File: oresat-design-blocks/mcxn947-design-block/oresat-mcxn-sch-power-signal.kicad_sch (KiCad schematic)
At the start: 64 parts, among them J1 BKUP-BATT, J3 CAN, J4 TERM, J5 10pin ARM SWD, J6 FTDI-UART-6PIN, SW1 RESET, SW2 ISP(BOOT), U1 MCXN947VKLT, U2 TCAN330, U3 TPS62111RSA, Y1 24 MHz, Y2 32.768 KHz

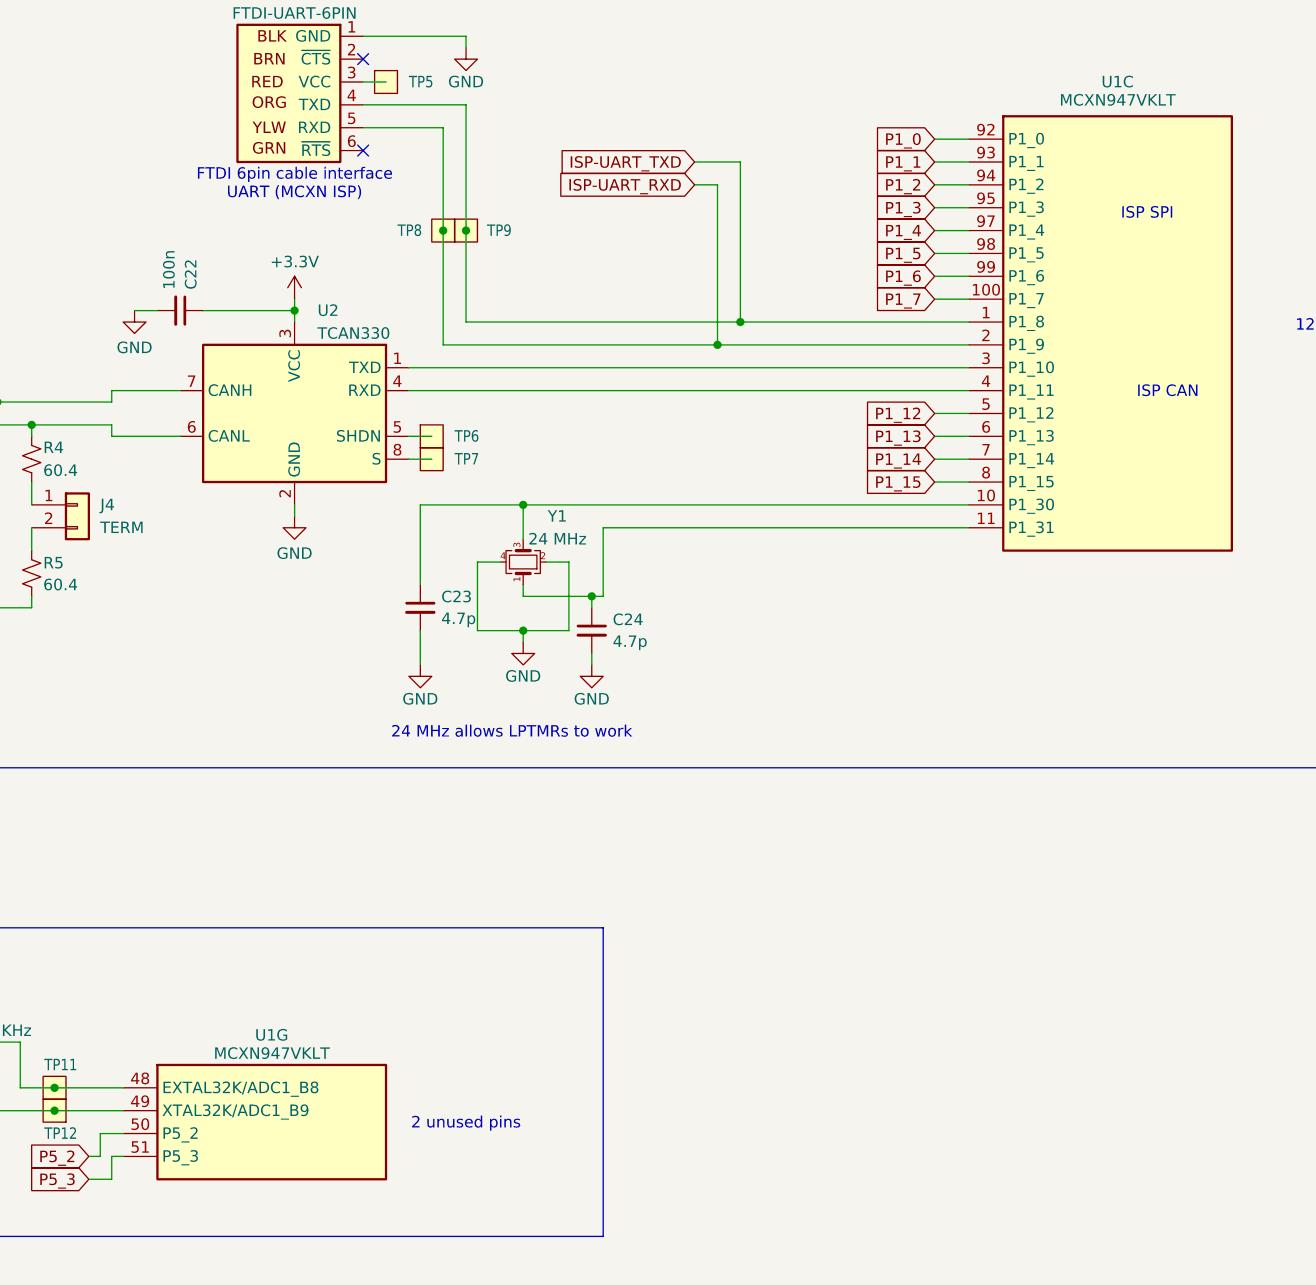
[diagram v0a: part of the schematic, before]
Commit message: updated MCXN board with new cap footprints, cleaned up routes
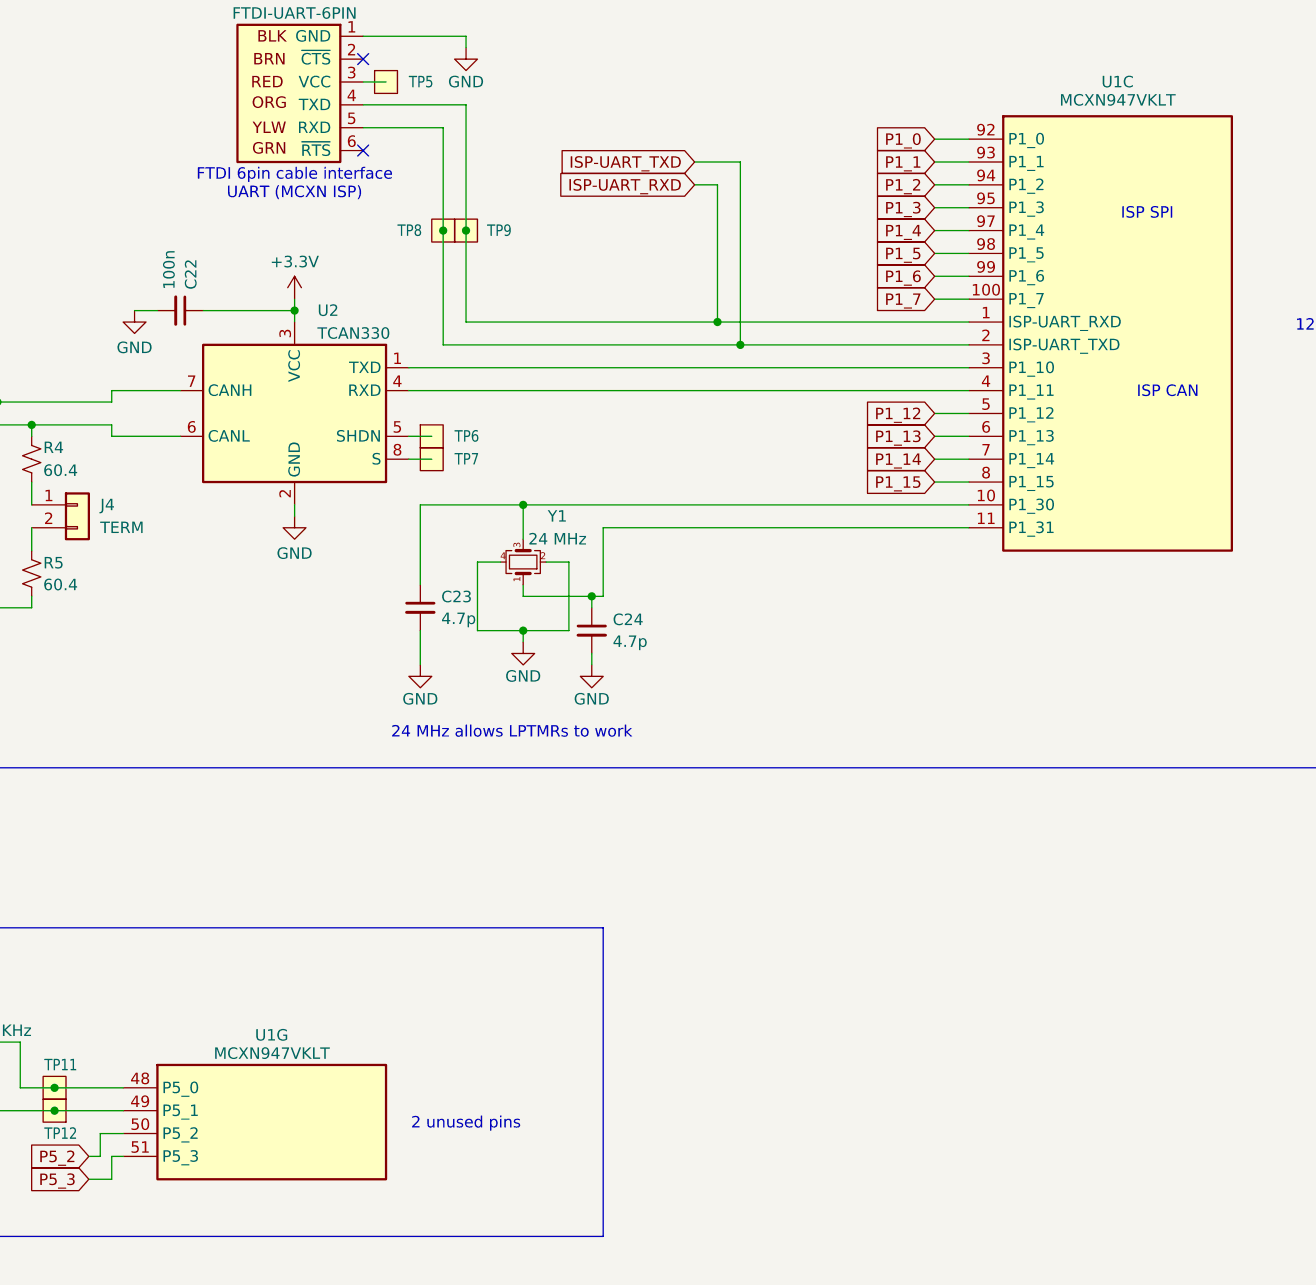
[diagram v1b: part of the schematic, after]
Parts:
- D1: footprint oresat-passives:PAT0816(0603) -> Package_TO_SOT_SMD:SOT-323_SC-70
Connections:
- net ISP-UART_RXD: now also J6.4 (TXD), TP9.1, U1.1 (P1_8); no longer J6.5 (RXD), TP8.1, U1.2 (P1_9)
- net ISP-UART_TXD: now also J6.5 (RXD), TP8.1, U1.2 (P1_9); no longer J6.4 (TXD), TP9.1, U1.1 (P1_8)
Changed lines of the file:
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@@
 	)
 	(junction
+		(at 311.15 157.48)
+		(diameter 0)
+		(color 0 0 0 0)
+	)
+	(junction
 		(at 81.28 166.37)
 		(diameter 0)
@@
 	)
 	(junction
-		(at 311.15 154.94)
-		(diameter 0)
-		(color 0 0 0 0)
-	)
-	(junction
 		(at 234.95 242.57)
 		(diameter 0)
@@
 	)
 	(junction
-		(at 81.28 168.91)
+		(at 308.61 154.94)
 		(diameter 0)
 		(color 0 0 0 0)
 	)
 	(junction
-		(at 81.28 176.53)
+		(at 81.28 168.91)
 		(diameter 0)
 		(color 0 0 0 0)
 	)
 	(junction
-		(at 299.72 55.88)
+		(at 81.28 176.53)
 		(diameter 0)
 		(color 0 0 0 0)
 	)
 	(junction
-		(at 308.61 157.48)
+		(at 299.72 55.88)
 		(diameter 0)
 		(color 0 0 0 0)
@@
 	(wire
 		(pts
-			(xy 278.13 157.48) (xy 308.61 157.48)
+			(xy 278.13 157.48) (xy 311.15 157.48)
 		)
 		(stroke
@@
 	(wire
 		(pts
-			(xy 308.61 139.7) (xy 308.61 157.48)
-		)
-		(stroke
-			(width 0)
-			(type default)
-		)
-	)
-	(wire
-		(pts
 			(xy 261.62 36.83) (xy 261.62 40.64)
 		)
@@
 	(wire
 		(pts
+			(xy 308.61 154.94) (xy 336.55 154.94)
+		)
+		(stroke
+			(width 0)
+			(type default)
+		)
+	)
+	(wire
+		(pts
 			(xy 280.67 130.81) (xy 280.67 144.78)
 		)
@@
 	(wire
 		(pts
+			(xy 311.15 157.48) (xy 336.55 157.48)
+		)
+		(stroke
+			(width 0)
+			(type default)
+		)
+	)
+	(wire
+		(pts
 			(xy 283.21 36.83) (xy 283.21 40.64)
 		)
@@
 	(wire
 		(pts
-			(xy 280.67 154.94) (xy 311.15 154.94)
+			(xy 280.67 154.94) (xy 308.61 154.94)
 		)
 		(stroke
@@
 	(wire
 		(pts
-			(xy 311.15 154.94) (xy 336.55 154.94)
-		)
-		(stroke
-			(width 0)
-			(type default)
-		)
-	)
-	(wire
-		(pts
 			(xy 240.03 245.11) (xy 242.57 245.11)
 		)
@@
 	(wire
 		(pts
+			(xy 311.15 137.16) (xy 311.15 157.48)
+		)
+		(stroke
+			(width 0)
+			(type default)
+		)
+	)
+	(wire
+		(pts
 			(xy 336.55 137.16) (xy 332.74 137.16)
 		)
@@
 	(wire
 		(pts
-			(xy 308.61 157.48) (xy 336.55 157.48)
-		)
-		(stroke
-			(width 0)
-			(type default)
-		)
-	)
-	(wire
-		(pts
 			(xy 82.55 106.68) (xy 82.55 109.22)
 		)
@@
 	(wire
 		(pts
-			(xy 311.15 137.16) (xy 311.15 154.94)
-		)
-		(stroke
-			(width 0)
-			(type default)
-		)
-	)
-	(wire
-		(pts
 			(xy 86.36 240.03) (xy 91.44 240.03)
 		)
@@
 	(wire
 		(pts
+			(xy 308.61 139.7) (xy 308.61 154.94)
+		)
+		(stroke
+			(width 0)
+			(type default)
+		)
+	)
+	(wire
+		(pts
 			(xy 241.3 247.65) (xy 242.57 247.65)
 		)
@@
 		)
 		(pin "49"
-			(alternate "XTAL32K/ADC1_B9")
 		)
 		(pin "50"
@@
 		)
 		(pin "48"
-			(alternate "EXTAL32K/ADC1_B8")
 		)
 		(pin "39"
@@
 			)
 		)
-		(property "Footprint" "oresat-passives:PAT0816(0603)"
+		(property "Footprint" "Package_TO_SOT_SMD:SOT-323_SC-70"
 			(at 62.865 179.705 0)
 			(effects
@@
 		)
 		(pin "1"
+			(alternate "ISP-UART_RXD")
 		)
 		(pin "3"
@@
 		)
 		(pin "2"
+			(alternate "ISP-UART_TXD")
 		)
 		(pin "95"

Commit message: Working on BOM
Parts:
- C4: MFR (none) -> Yageo; MPN (none) -> CC0603KRX5R7BB105
- C5: MPN CL21B106KOQNNNG -> CL10X106MO8NRNC
- C6: MFR (none) -> Samsung; MPN (none) -> CL10A225KO8NNNC
- R10: MFR Panasonic -> Samsung; MPN ERA-3AEB272V -> RC1005F6653CS
- R3, R6, R7, R8, R9: MFR (none) -> Samsung; MPN (none) -> RC1005F6653CS
- U2: MFR (none) -> Texas Instruments
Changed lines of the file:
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@@
 			)
 		)
+		(property "MFR" "Samsung"
+			(at 254 43.18 0)
+			(effects
+				(font
+					(size 1.27 1.27)
+				)
+				(hide yes)
+			)
+		)
+		(property "MPN" "RC1005F6653CS"
+			(at 254 43.18 0)
+			(effects
+				(font
+					(size 1.27 1.27)
+				)
+				(hide yes)
+			)
+		)
 		(pin "1"
 		)
@@
 			)
 		)
-		(property "Datasheet" "~"
+		(property "Datasheet" "https://mm.digikey.com/Volume0/opasdata/d220001/medias/docus/43/CL10X106MO8NRNC_Spec.pdf"
 			(at 39.37 82.55 0)
 			(effects
@@
 			)
 		)
-		(property "Description" "Unpolarized capacitor"
+		(property "Description" "10 µF ±20% 16V Ceramic Capacitor X6S 0603 (1608 Metric)"
 			(at 39.37 82.55 0)
 			(effects
@@
 			)
 		)
-		(property "MPN" "CL21B106KOQNNNG"
+		(property "MPN" "CL10X106MO8NRNC"
 			(at 39.37 82.55 0)
 			(effects
@@
 			)
 		)
+		(property "MFR" "Samsung"
+			(at 143.51 144.78 0)
+			(effects
+				(font
+					(size 1.27 1.27)
+				)
+				(hide yes)
+			)
+		)
+		(property "MPN" "RC1005F6653CS"
+			(at 143.51 144.78 0)
+			(effects
+				(font
+					(size 1.27 1.27)
+				)
+				(hide yes)
+			)
+		)
 		(pin "1"
 		)
@@
 			)
 		)
-		(property "Description" "Unpolarized capacitor, small symbol"
+		(property "Description" "2.2 µF ±10% 16V Ceramic Capacitor X5R 0603 (1608 Metric)"
+			(at 58.42 222.25 0)
+			(effects
+				(font
+					(size 1.27 1.27)
+				)
+				(hide yes)
+			)
+		)
+		(property "MFR" "Samsung"
+			(at 58.42 222.25 0)
+			(effects
+				(font
+					(size 1.27 1.27)
+				)
+				(hide yes)
+			)
+		)
+		(property "MPN" "CL10A225KO8NNNC"
 			(at 58.42 222.25 0)
 			(effects
@@
 			)
 		)
+		(property "MFR" "Texas Instruments"
+			(at 261.62 165.1 0)
+			(effects
+				(font
+					(size 1.27 1.27)
+				)
+				(hide yes)
+			)
+		)
 		(pin "4"
 		)
@@
 			)
 		)
+		(property "MFR" "Yageo"
+			(at 50.8 208.28 0)
+			(effects
+				(font
+					(size 1.27 1.27)
+				)
+				(hide yes)
+			)
+		)
+		(property "MPN" "CC0603KRX5R7BB105"
+			(at 50.8 208.28 0)
+			(effects
+				(font
+					(size 1.27 1.27)
+				)
+				(hide yes)
+			)
+		)
 		(pin "2"
 		)
@@
 			)
 		)
-		(property "MFR" "Panasonic"
+		(property "MFR" "Samsung"
 			(at 138.43 82.55 0)
 			(effects
@@
 			)
 		)
-		(property "MPN" "ERA-3AEB272V"
+		(property "MPN" "RC1005F6653CS"
 			(at 138.43 82.55 0)
 			(effects
@@
 			)
 		)
+		(property "MFR" "Samsung"
+			(at 283.21 43.18 0)
+			(effects
+				(font
+					(size 1.27 1.27)
+				)
+				(hide yes)
+			)
+		)
+		(property "MPN" "RC1005F6653CS"
+			(at 283.21 43.18 0)
+			(effects
+				(font
+					(size 1.27 1.27)
+				)
+				(hide yes)
+			)
+		)
 		(pin "1"
 		)
@@
 			)
 		)
+		(property "MFR" "Samsung"
+			(at 261.62 43.18 0)
+			(effects
+				(font
+					(size 1.27 1.27)
+				)
+				(hide yes)
+			)
+		)
+		(property "MPN" "RC1005F6653CS"
+			(at 261.62 43.18 0)
+			(effects
+				(font
+					(size 1.27 1.27)
+				)
+				(hide yes)
+			)
+		)
 		(pin "1"
 		)
@@
 			(at 254 66.04 0)
 			(effects
+				(font
+					(size 1.27 1.27)
+				)
+				(hide yes)
+			)
+		)
+		(property "MFR" "Samsung"
+			(at 254 66.04 0)
+			(effects
+				(font
+					(size 1.27 1.27)
+				)
+				(hide yes)
+			)
+		)
+		(property "MPN" "RC1005F6653CS"
+			(at 254 66.04 0)
+			(effects

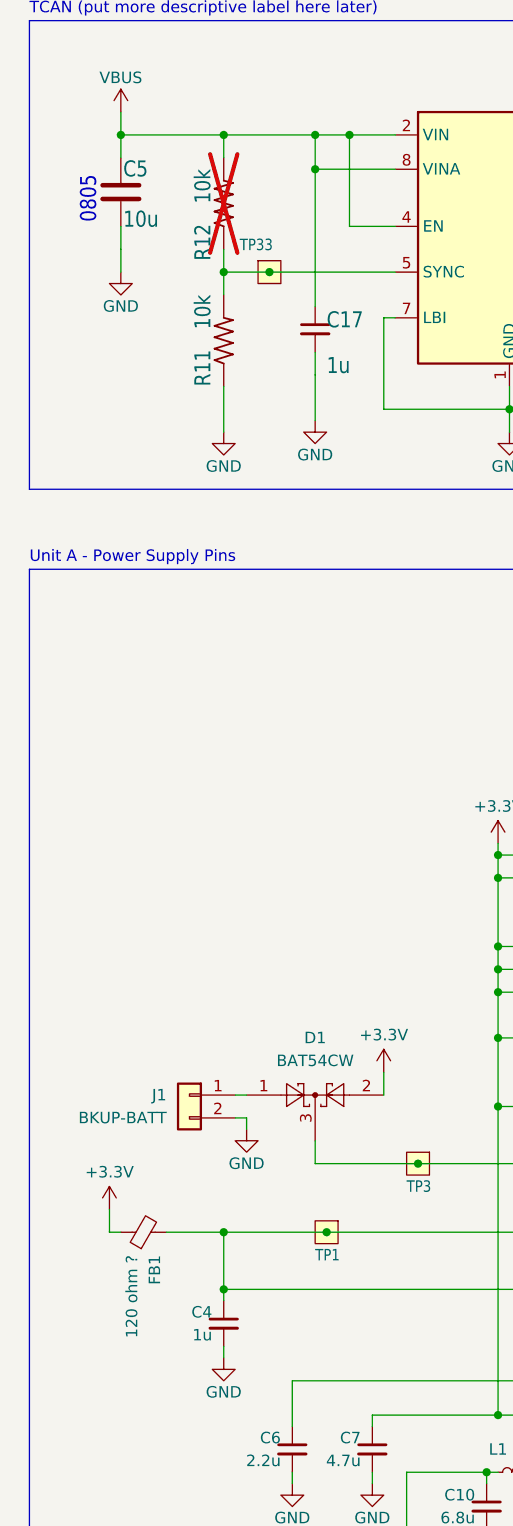
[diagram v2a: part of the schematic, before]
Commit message: Updated BOM with MPNs and fixed one missing 0805 footprint error, rev'd board to v1.1
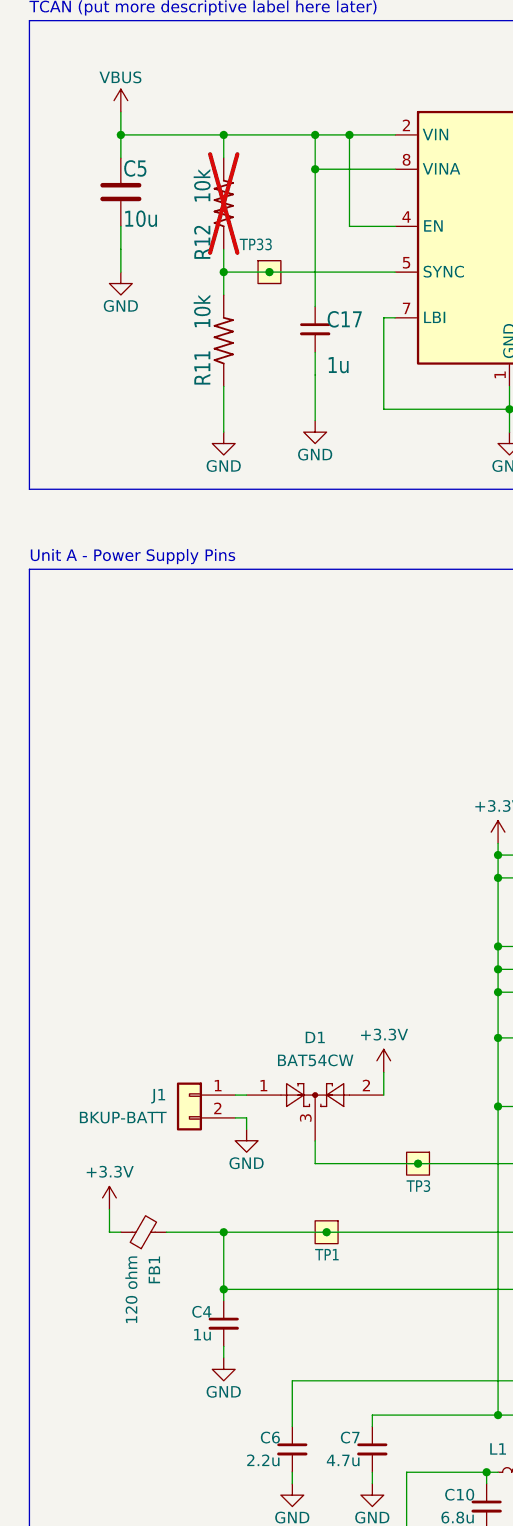
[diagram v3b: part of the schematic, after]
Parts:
- C10: MFR (none) -> Murata Electronics; MPN (none) -> GCJ31CR71A685KA13L
- C11, C7: MFR (none) -> Murata Electronics; MPN (none) -> GRM188R61E475KE11D
- C12, C13, C14, C15, C16, C2, C20, C22, C3, C8, C9: MFR (none) -> Murata Electronics; MPN (none) -> GRM188R72A104KA35D
- C17, C4: MFR Yageo -> Murata Electronics; MPN CC0603KRX5R7BB105 -> GRM185R61E105KA12J
- C18: footprint oresat-passives:0603-C-NOSILK -> oresat-passives:0805-C-NOSILK; MFR Murata -> Murata Electronics; MPN GRM21BD71A226ME44L -> GRM21BR61E226ME44L
- C23, C24, C25, C26: MFR (none) -> Murata Electronics; MPN (none) -> GRM1885C1H4R7WA01D
- C5: MFR Samsung -> Murata Electronics; MPN CL10X106MO8NRNC -> GRM188R61E106KA73D
- C6: MFR Samsung -> Murata Electronics; MPN CL10A225KO8NNNC -> GRM188R61E225KA12D
- D1: MFR (none) -> Nexperia; MPN (none) -> BAT54CW,115
- FB1: value 120 ohm ? -> 120 ohm; MFR (none) -> Fair-Rite; MPN (none) -> 2508051217Y6
- J1, J4: MFR (none) -> Adam Tech; MPN (none) -> PH1-02-UA
- J3: MFR (none) -> Adam Tech; MPN (none) -> PH1-04-UA
- J5: MFR (none) -> GCT; MPN (none) -> BD120-10-A-0305-0229-L-B
- J6: MFR (none) -> Adam Tech; MPN (none) -> PH1-06-UA
- R10, R11, R3, R6, R7, R8, R9: MFR Samsung -> Stackpole Electronics Inc; MPN RC1005F6653CS -> RMCF0603FT10K0
- R4, R5: MFR (none) -> Stackpole Electronics Inc; MPN (none) -> RMCF0603FT60R4
- SW1, SW2: MFR (none) -> OMRON; MPN (none) -> B3F-1000
- U2: MPN (none) -> TCAN330DCNR
- U3: MPN TPS62111RSA -> TPS62111RSAR
